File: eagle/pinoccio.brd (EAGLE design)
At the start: 25.4 x 50.8 mm, 50 parts, among them Q1 16MHz, Q2 32.768k, Q4 MOSFET-PCHANNEL, Q5 TRANSISTOR-NPN-DUAL, U1 MCP73831, U2 3.3V, U4 ATMEGA128RFA1, X1 USB-MICROB, Y2 ANTENNA2SMD5

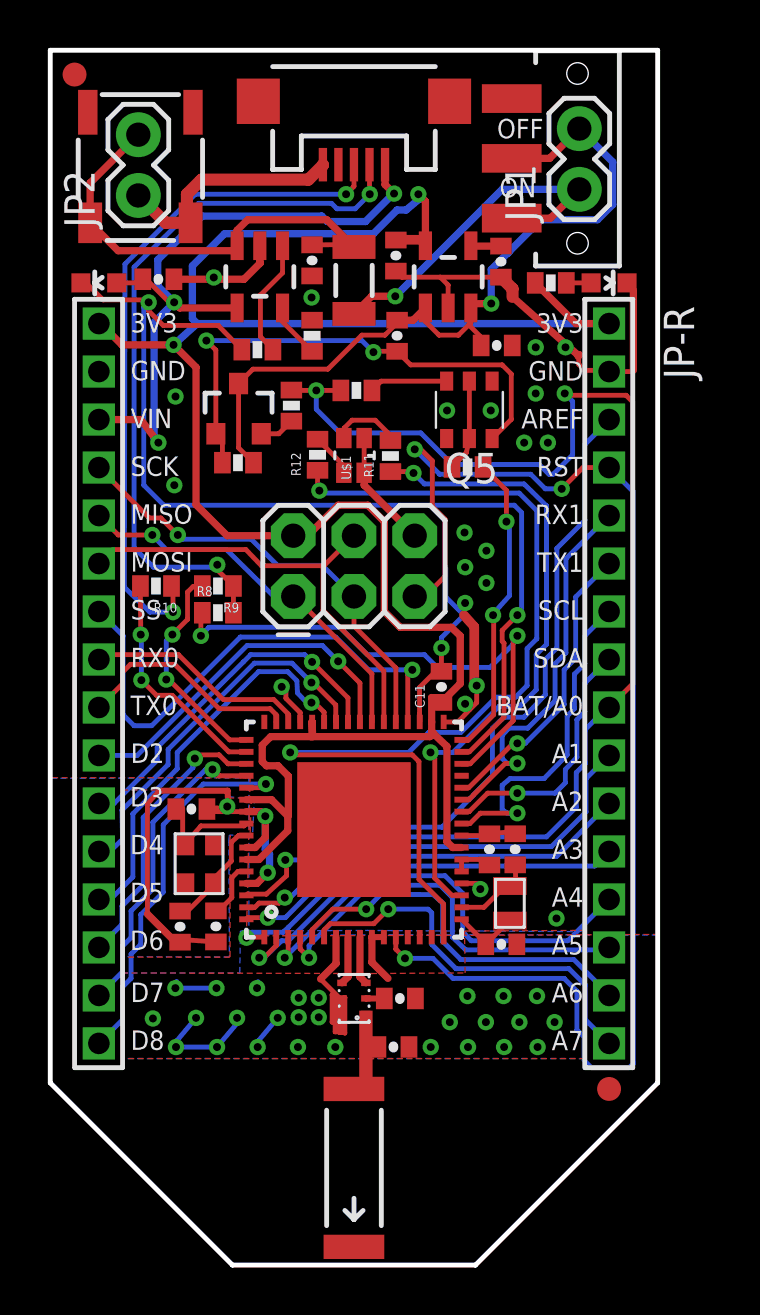
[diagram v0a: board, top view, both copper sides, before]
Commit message: Removed D1 LED for power--for better power handling.  Instead, will modify the bootloader to flash the bicolor LED a couple times upon power up, then turn off.  Thanks Louis for the idea!
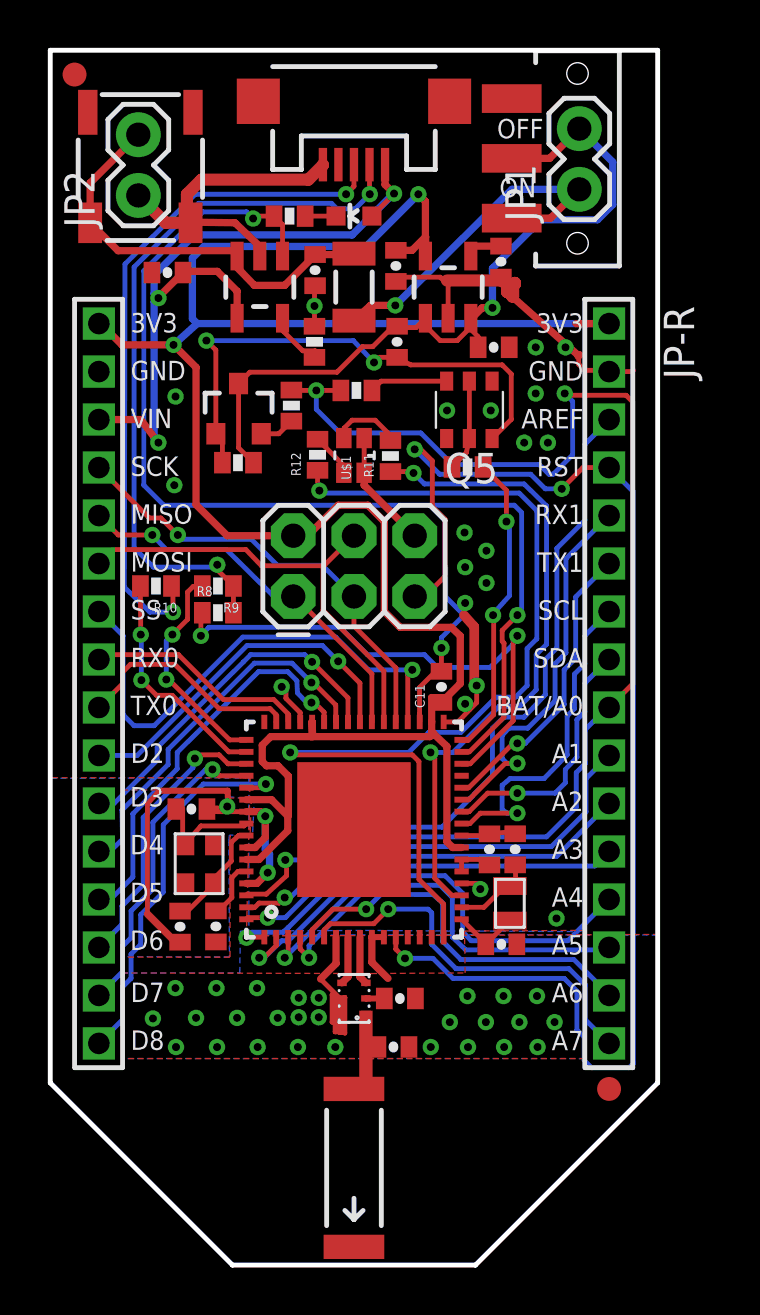
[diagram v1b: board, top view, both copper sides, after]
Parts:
- removed D1: Green, SparkFun:LED-0603
- removed R2: 1k, SparkFun:0402-RES
- moved D2 11.0 mm to (12.7, 43.9)
- moved R3 5.75 mm to (10.0, 43.9), turned to 0 degrees
- moved C4 0.47 mm to (4.90, 41.5), turned to 180 degrees
- moved U1 0.43 mm to (8.76, 40.9)
- moved U2 0.43 mm to (16.6, 40.9)
- moved C2 0.43 mm to (14.5, 41.8)
- moved C5 0.43 mm to (11.1, 41.6)
- moved F1 0.28 mm to (12.7, 40.9)
- moved R4 0.27 mm to (11.0, 38.6)
- moved C1 0.25 mm to (14.5, 38.6)
- moved C6 0.15 mm to (18.5, 38.4)
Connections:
- removed net N$14: R3.1, U1.1
- net CHGSTATUS: now also R3.1, U1.1; no longer D2.C, R3.2
- net GND: no longer D1.C
- net N$22: now also D2.C, R3.2; no longer D1.A, R2.2
- net VCC: no longer R2.1
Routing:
- net GND: track 99.2 -> 87.8 mm, vias 52 -> 51
- net N$14: track 4.94 -> 0.00 mm
- net VCC: track 96.7 -> 93.2 mm
- net CHGSTATUS: track 43.7 -> 45.0 mm
- net VBAT: track 19.4 -> 18.5 mm

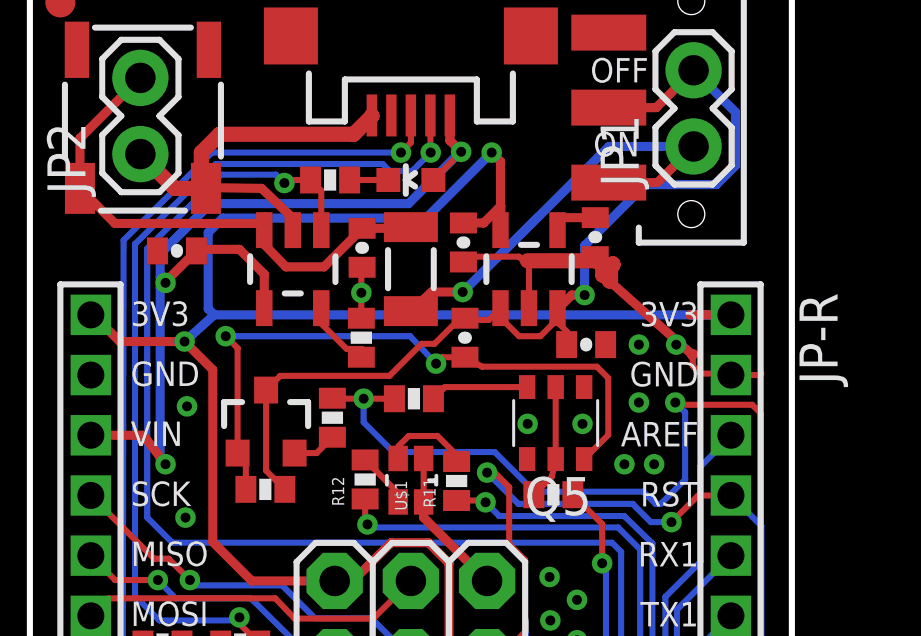
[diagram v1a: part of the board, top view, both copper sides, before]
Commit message: Clean up bottom silkscreen
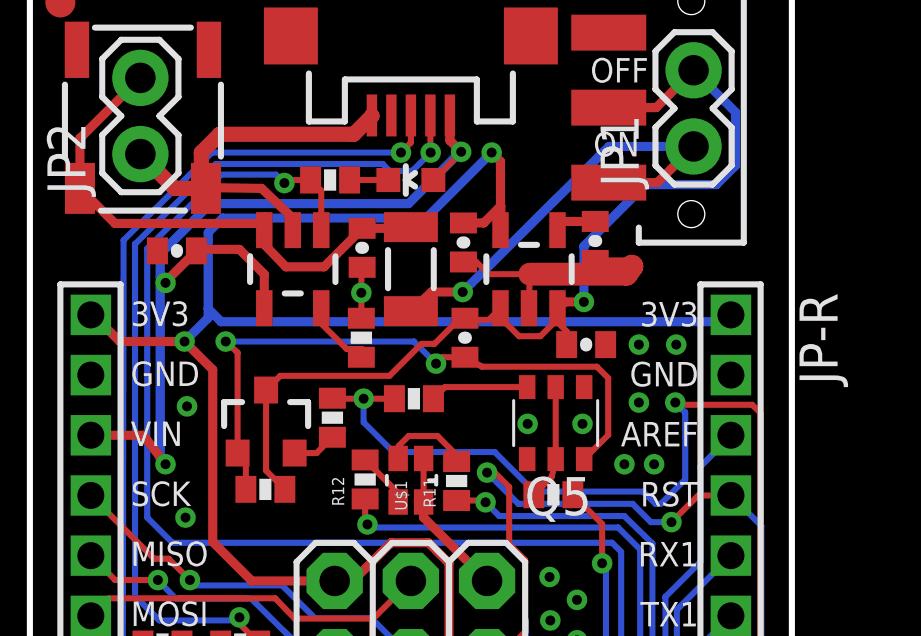
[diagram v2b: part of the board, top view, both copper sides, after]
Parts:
- moved C3 0.13 mm to (18.8, 41.8)
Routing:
- net GND: track 87.8 -> 81.0 mm
- net VCC: track 93.2 -> 92.1 mm

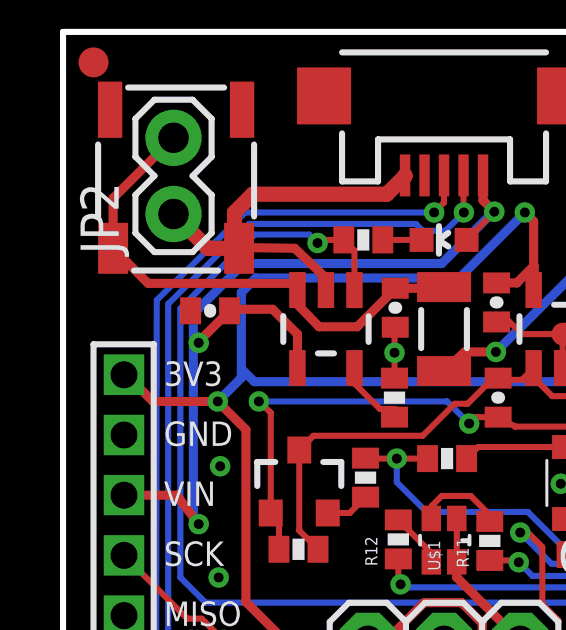
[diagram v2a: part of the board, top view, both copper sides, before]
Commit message: Add a couple more ground vias to minimize impedance
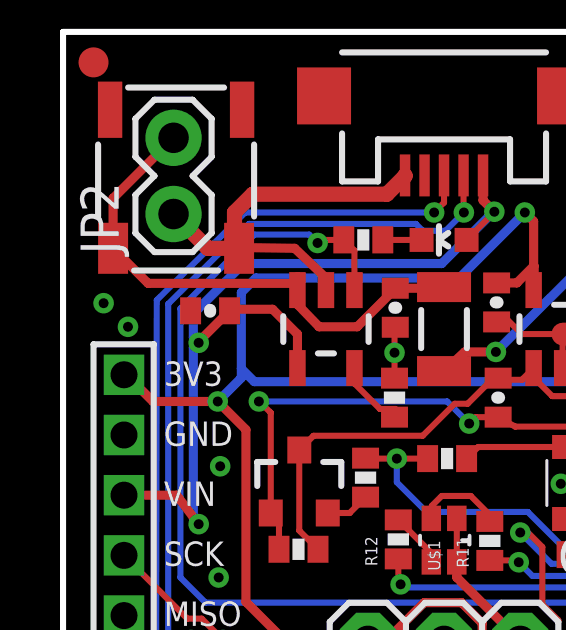
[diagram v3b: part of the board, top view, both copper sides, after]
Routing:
- net GND: vias 51 -> 53
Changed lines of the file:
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@@
 <wire x1="15.2908" y1="40.7266" x2="16.6624" y2="40.7266" width="0.2032" layer="1"/>
 <wire x1="13.9458" y1="13.716" x2="13.95" y2="13.7118" width="0" layer="19" extent="1-1"/>
+<via x="1.3518" y="41.7568" extent="1-16" drill="0.3302"/>
+<via x="2.1646" y="40.9694" extent="1-16" drill="0.3302"/>
 </signal>
 <signal name="VCC" class="1">

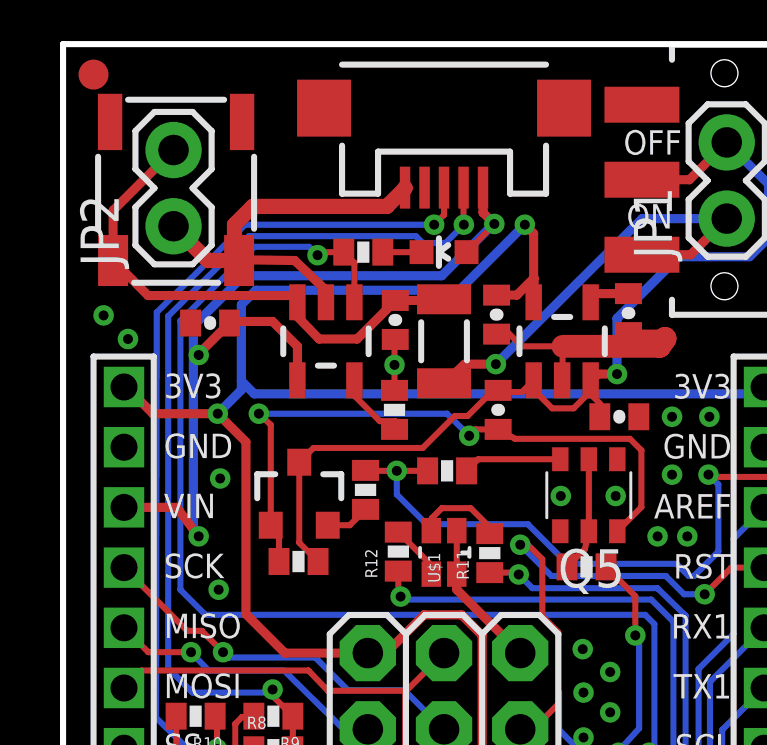
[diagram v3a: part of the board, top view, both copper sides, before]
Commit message: Updated bicolor LED values to a more sane value.  Add 0603 landing pattern for Lipo IC charge current capacity (for people to mod if they want higher C-ratings).  Fix mosfet reversal error.  (Thanks Monty!)
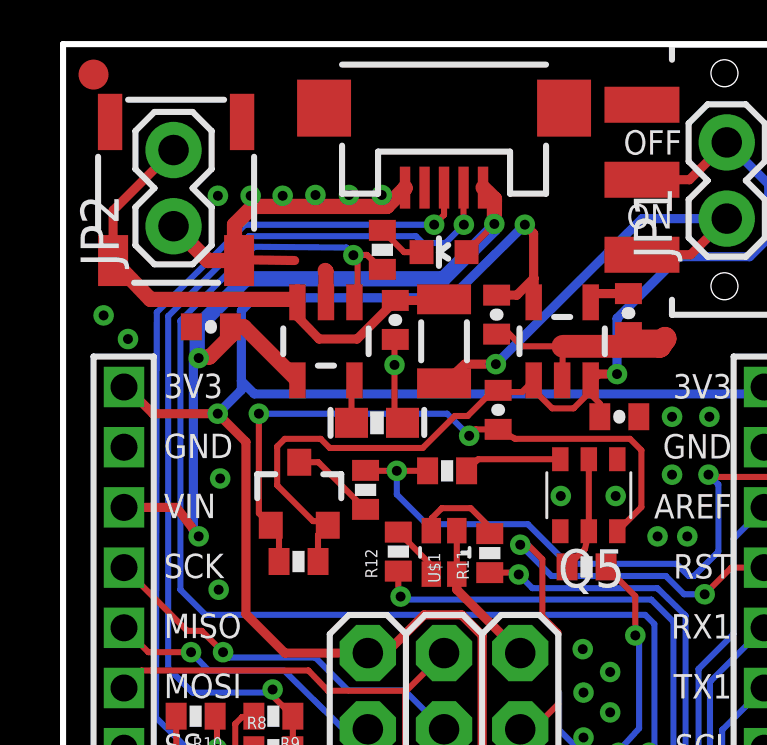
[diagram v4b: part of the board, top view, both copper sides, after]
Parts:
- Q4: device SparkFun:SOT23-3 -> Pinoccio:SOT23-3
- R11, R12: value 68 -> 1K
- R4: device SparkFun:0402-RES -> SparkFun:0603-RES
- moved R4 0.73 mm to (10.5, 38.2), turned to 0 degrees
- moved R3 0.64 mm to (10.6, 43.9), turned to 90 degrees
- moved C4 0.13 mm to (4.93, 41.4)
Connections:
- net N$3: now also Q4.3; no longer Q4.2
- net VBAT-AF: now also Q4.2; no longer Q4.3
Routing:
- net VBAT-AF: track 33.0 -> 35.1 mm
- net N$3: track 1.48 -> 2.86 mm
- net CHGSTATUS: track 45.0 -> 46.3 mm
- net N$11: track 2.50 -> 1.46 mm
- net USB_VIN: track 29.8 -> 29.0 mm
- net GND: track 81.0 -> 81.4 mm, vias 53 -> 59

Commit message: Updated datasheet to dual package transistor.
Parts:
- R4: device SparkFun:0603-RES -> SparkFun:0402-RES
- moved R4 0.18 mm to (10.3, 38.2)
- moved C7 0.15 mm to (6.90, 14.0)
- moved C12 0.15 mm to (5.43, 14.0)
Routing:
- net GND: track 81.4 -> 78.0 mm

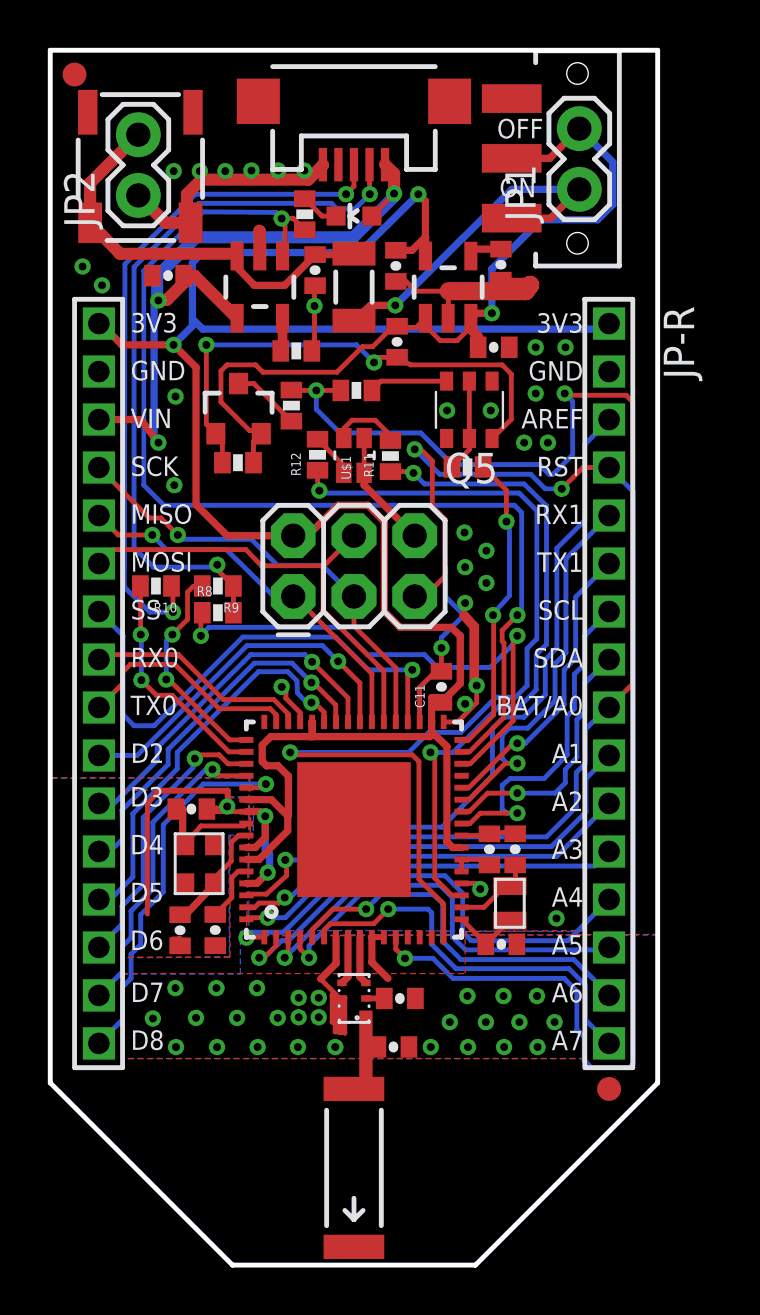
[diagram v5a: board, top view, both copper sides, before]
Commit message: Update package for right-angle switch, make minor changes as recommended in Atmel App Note AVR2044
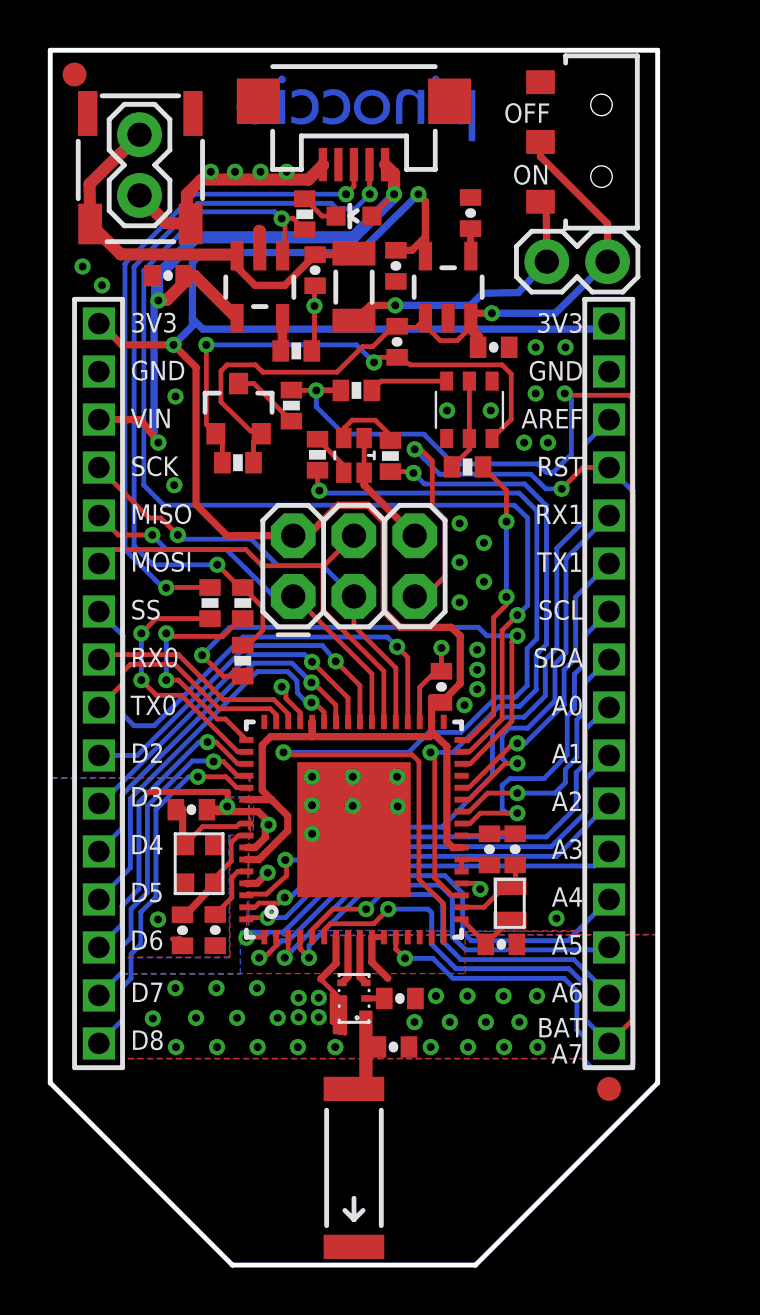
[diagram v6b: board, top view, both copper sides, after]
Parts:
- added U$2: (no value), Pinoccio:LOGO-PINOCCIO-COPPER
- added U$3: (no value), Pinoccio:LOGO-PINOCCIO-STOP
- added U$6: (no value), Pinoccio:LOGO-OSHW-SS
- C11: value 2uF -> 2.2uF
- S2: device SparkFun:SWITCH-SPDT-SMD -> Pinoccio:SWITCH-SPDT-SMD
- moved JP1 3.31 mm to (20.8, 42.0), turned to 0 degrees
- moved C3 2.50 mm to (17.6, 44.0), turned to 90 degrees
- moved R10 2.37 mm to (6.68, 27.7), turned to 270 degrees
- moved R8 2.26 mm to (8.05, 25.3), turned to 90 degrees
- moved R9 1.26 mm to (8.05, 27.7), turned to 270 degrees
- moved S2 1.22 mm to (23.1, 47.0)
- moved C12 0.10 mm to (5.53, 14.0)
- moved JP2 0.05 mm to (3.73, 44.7)
- moved BATT 0.05 mm to (1.17, 48.9)
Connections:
- net A0: no longer R5.1, R7.2
- net A7: now also R5.1, R7.2
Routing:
- net A7: track 16.5 -> 65.3 mm, vias 1 -> 3
- net A0: track 54.2 -> 20.3 mm, vias 3 -> 1
- net GND: track 78.0 -> 52.3 mm, vias 59 -> 68
- net N$8: track 15.0 -> 11.7 mm
- net VBAT-AF: track 35.1 -> 32.4 mm
- net N$9: track 30.5 -> 32.8 mm
- net VCC: track 92.0 -> 90.7 mm
- net USBD+: track 9.58 -> 10.7 mm
- net N$43: track 28.9 -> 28.0 mm
- net D8: track 16.1 -> 15.3 mm
- net D7: track 13.1 -> 13.9 mm
- net USBD-: track 9.15 -> 9.90 mm
- net D6: track 11.9 -> 12.7 mm
- net LED-RED: track 42.2 -> 42.7 mm
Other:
- board text added: "/Volumes/Data/Users/eric/Desktop/Untitled-1.bmp"
- board text added: "A0"
- board text removed: "BAT/A0"
- board text removed: "Pinoccio v0.5"
- board text removed: "SW"

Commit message: Moar ground routing/vias to decrease any possible inductance
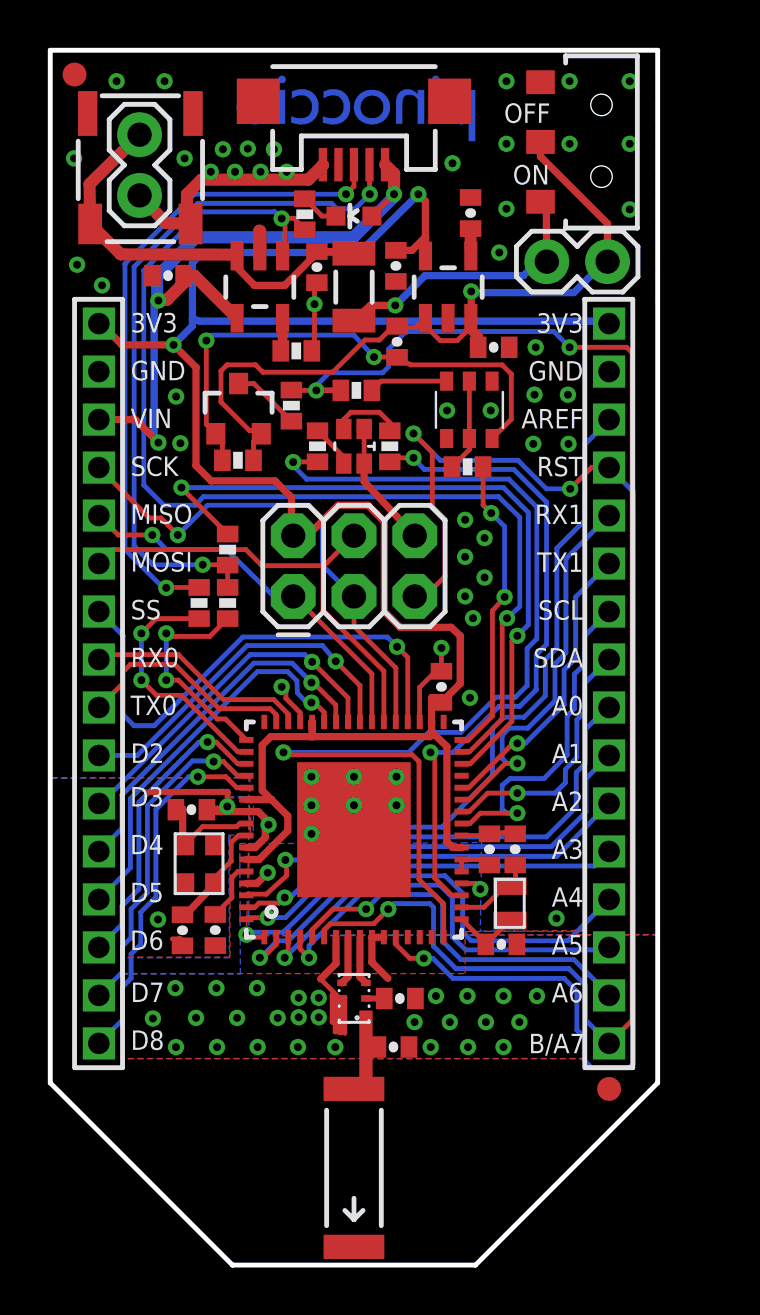
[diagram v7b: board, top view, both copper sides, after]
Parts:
- moved U$6 37.5 mm to (14.1, 41.1)
- moved R8 4.69 mm to (7.42, 29.9), turned to 270 degrees
- moved R9 0.63 mm to (7.42, 27.7)
- moved R10 0.46 mm to (6.22, 27.7)
- moved R11 0.41 mm to (14.2, 34.2)
- moved U$1 0.38 mm to (12.7, 34.2)
- moved R12 0.36 mm to (11.2, 34.2)
- moved C5 0.15 mm to (11.2, 41.7)
- moved R6 0.10 mm to (7.85, 33.7)
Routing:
- net USBENABLE: track 22.4 -> 29.5 mm
- net N$9: track 32.8 -> 29.5 mm
- net SCK: track 18.9 -> 21.3 mm
- net LED-RED: track 42.7 -> 44.7 mm
- net VBAT: track 18.8 -> 19.8 mm
- net A7: track 65.3 -> 64.4 mm
- net RESET: track 56.2 -> 57.0 mm
- net USBD-: track 9.90 -> 9.27 mm
- net VBAT-AF: track 32.4 -> 33.0 mm
- net GND: track 52.3 -> 52.8 mm, vias 68 -> 82
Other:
- board text added: "B/A7"
- board text removed: "A7"
- board text removed: "BAT"
- board text removed: "CERN OHL v.1.1"
- board text removed: "Licensed under"
